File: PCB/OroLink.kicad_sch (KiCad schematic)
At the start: 8 parts, among them J1 67996-408HLF

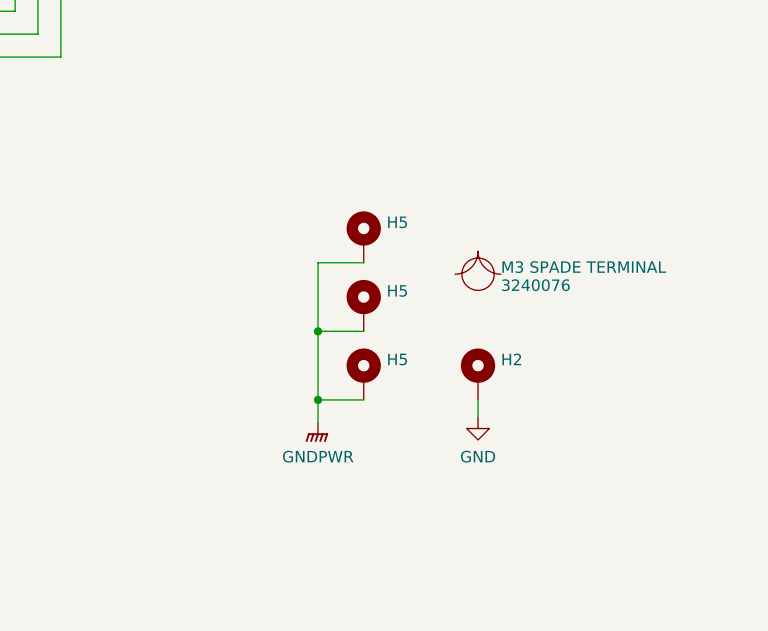
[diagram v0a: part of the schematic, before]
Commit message: add 1nf 3kv caps to GNDPWR mounting holes (closes #29)
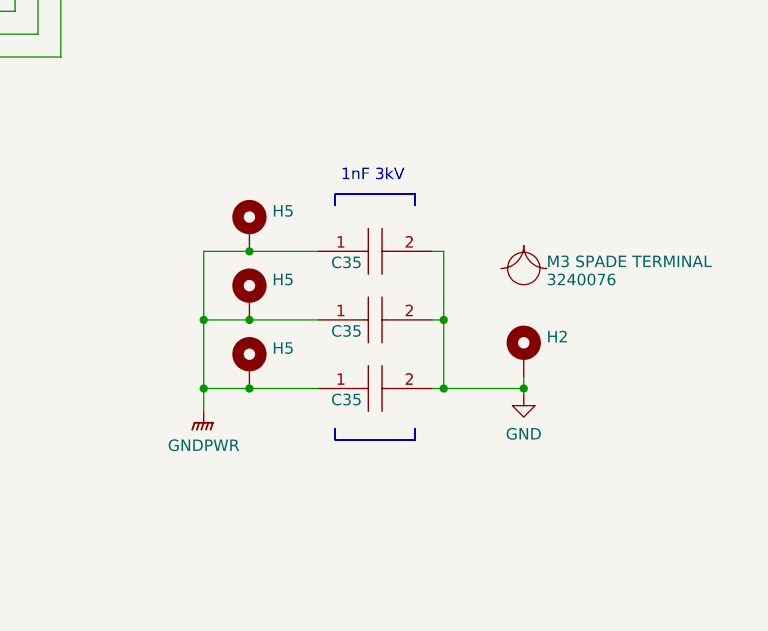
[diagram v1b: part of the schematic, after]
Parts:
- added C35 (x3): 1nF 5kV, CAPC5664X270N, symbol SamacSys_Parts:HV2225Y102KXMATHV
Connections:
- net GND: now also C35.2, C35.2, C35.2
- net GNDPWR: now also C35.1, C35.1, C35.1
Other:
- note added: "1nF 3kV"
- moved on the sheet: H2, H5

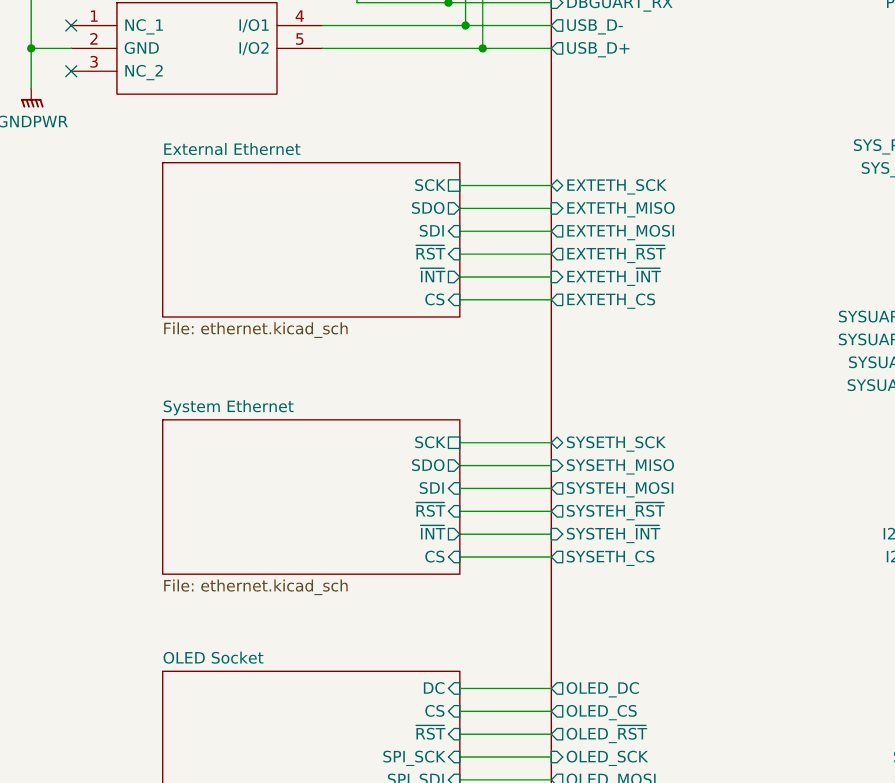
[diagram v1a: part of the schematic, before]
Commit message: switch to self-contained magnetics ethernet jack (closes #28)
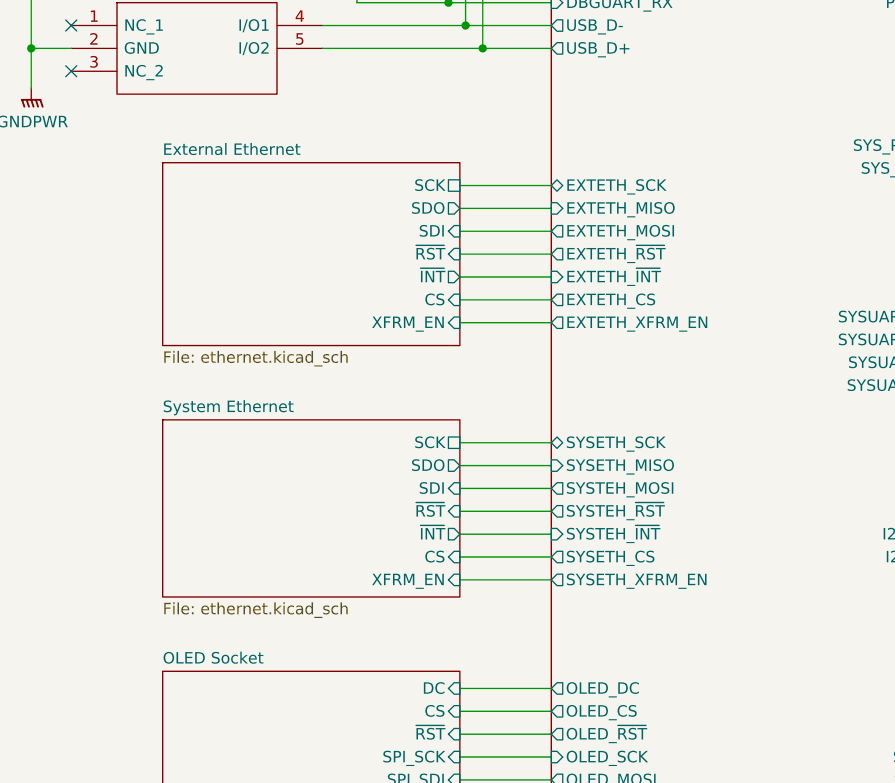
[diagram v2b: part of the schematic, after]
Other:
- sheet External Ethernet ports: added XFRM_EN; removed none
- sheet Microcontroller ports: added EXTETH_XFRM_EN, SYSETH_XFRM_EN; removed none
- sheet System Ethernet ports: added XFRM_EN; removed none
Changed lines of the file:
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@@
+    (stroke (width 0) (type default))
+  )
+  (wire (pts (xy 73.66 119.38) (xy 83.82 119.38))
     (stroke (width 0) (type default))
   )
@@
   )
   (wire (pts (xy 73.66 85.725) (xy 83.82 85.725))
+    (stroke (width 0) (type default))
+  )
+  (wire (pts (xy 73.66 90.805) (xy 83.82 90.805))
     (stroke (width 0) (type default))
   )
@@
     )
   )
-  (sheet (at 40.64 101.6) (size 33.02 17.145) (fields_autoplaced)
+  (sheet (at 40.64 101.6) (size 33.02 19.685) (fields_autoplaced)
     (stroke (width 0.1524) (type solid))
     (fill (color 0 0 0 0.0000))
@@
       (effects (font (size 1.27 1.27)) (justify left bottom))
     )
-    (property "Sheetfile" "ethernet.kicad_sch" (at 40.64 119.3296 0)
+    (property "Sheetfile" "ethernet.kicad_sch" (at 40.64 121.8696 0)
       (effects (font (size 1.27 1.27)) (justify left top))
     )
@@
     )
     (pin "CS" input (at 73.66 116.84 0)
+      (effects (font (size 1.27 1.27)) (justify right))
+    )
+    (pin "XFRM_EN" input (at 73.66 119.38 0)
       (effects (font (size 1.27 1.27)) (justify right))
     )
@@
     )
   )
-  (sheet (at 40.64 73.025) (size 33.02 17.145) (fields_autoplaced)
+  (sheet (at 40.64 73.025) (size 33.02 20.32) (fields_autoplaced)
     (stroke (width 0.1524) (type solid))
     (fill (color 0 0 0 0.0000))
@@
       (effects (font (size 1.27 1.27)) (justify left bottom))
     )
-    (property "Sheetfile" "ethernet.kicad_sch" (at 40.64 90.7546 0)
+    (property "Sheetfile" "ethernet.kicad_sch" (at 40.64 93.9296 0)
       (effects (font (size 1.27 1.27)) (justify left top))
     )
@@
     )
     (pin "CS" input (at 73.66 88.265 0)
+      (effects (font (size 1.27 1.27)) (justify right))
+    )
+    (pin "XFRM_EN" input (at 73.66 90.805 0)
       (effects (font (size 1.27 1.27)) (justify right))
     )
@@
       (effects (font (size 1.27 1.27)) (justify left))
     )
+    (pin "SYSETH_XFRM_EN" output (at 83.82 119.38 180)
+      (effects (font (size 1.27 1.27)) (justify left))
+    )
+    (pin "EXTETH_XFRM_EN" output (at 83.82 90.805 180)
+      (effects (font (size 1.27 1.27)) (justify left))
+    )

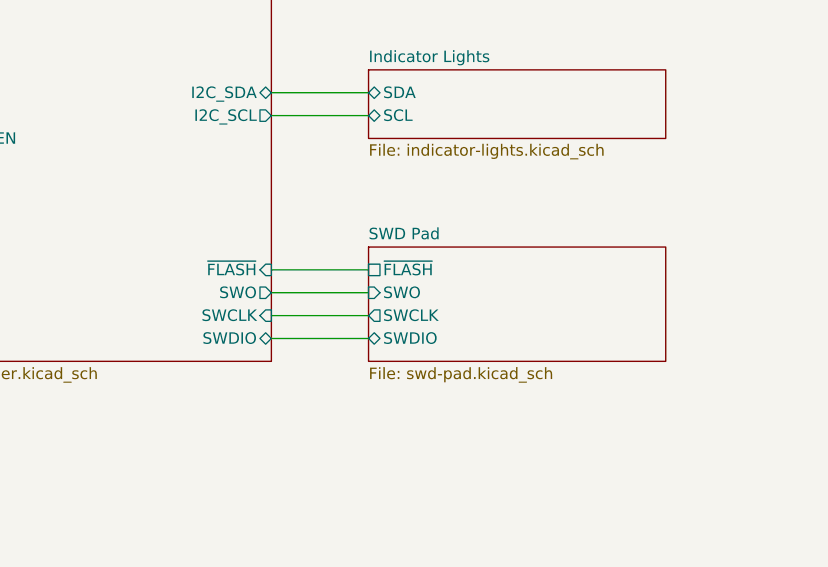
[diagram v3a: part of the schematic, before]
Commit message: add pullup/down resistors and fix oro 6p lines with boot1/0
closes #24
closes #21
closes #15
closes #12
closes #6
closes #3
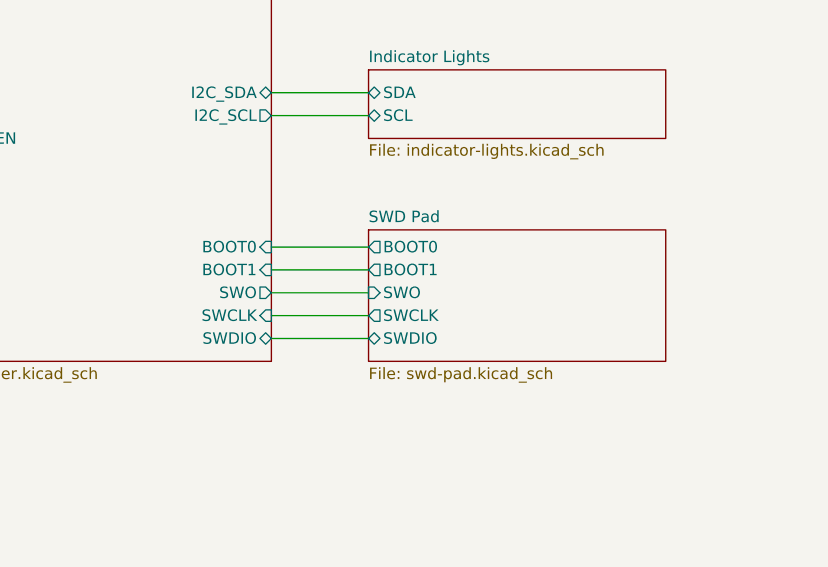
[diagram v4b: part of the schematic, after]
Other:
- sheet Microcontroller ports: added BOOT0, BOOT1; removed ~{FLASH}
- sheet SWD Pad ports: added BOOT0, BOOT1; removed ~{FLASH}
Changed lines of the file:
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@@
+    (stroke (width 0) (type default))
+  )
+  (wire (pts (xy 129.54 131.445) (xy 140.335 131.445))
     (stroke (width 0) (type default))
   )
@@
     )
   )
-  (sheet (at 140.335 131.445) (size 33.02 12.7)
+  (sheet (at 140.335 129.54) (size 33.02 14.605)
     (stroke (width 0.1524) (type solid))
     (fill (color 0 0 0 0.0000))
-    (property "Sheetname" "SWD Pad" (at 140.335 130.7334 0)
+    (property "Sheetname" "SWD Pad" (at 140.335 128.8284 0)
       (effects (font (size 1.27 1.27)) (justify left bottom))
     )
@@
       (effects (font (size 1.27 1.27)) (justify left top))
     )
-    (pin "~{FLASH}" passive (at 140.335 133.985 180)
-      (effects (font (size 1.27 1.27)) (justify left))
-    )
     (pin "SWO" input (at 140.335 136.525 180)
       (effects (font (size 1.27 1.27)) (justify left))
@@
     )
     (pin "SWDIO" bidirectional (at 140.335 141.605 180)
+      (effects (font (size 1.27 1.27)) (justify left))
+    )
+    (pin "BOOT1" output (at 140.335 133.985 180)
+      (effects (font (size 1.27 1.27)) (justify left))
+    )
+    (pin "BOOT0" output (at 140.335 131.445 180)
       (effects (font (size 1.27 1.27)) (justify left))
     )
@@
       (effects (font (size 1.27 1.27)) (justify right))
     )
-    (pin "~{FLASH}" input (at 129.54 133.985 0)
-      (effects (font (size 1.27 1.27)) (justify right))
-    )
     (pin "OLED_MOSI" output (at 83.82 141.605 180)
       (effects (font (size 1.27 1.27)) (justify left))
@@
       (effects (font (size 1.27 1.27)) (justify left))
     )
-    (instances
+    (pin "BOOT0" input (at 129.54 131.445 0)
+      (effects (font (size 1.27 1.27)) (justify right))
+    )
+    (pin "BOOT1" input (at 129.54 133.985 0)
+      (effects (font (size 1.27 1.27)) (justify right))
+    )
+    (instances

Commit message: switch to smaller package for 1nF 3kV caps (closes #33)
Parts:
- C35: footprint CAPC5664X270N -> CAPC4620X220N; symbol SamacSys_Parts:HV2225Y102KXMATHV -> SamacSys_Parts:885342210004; Height 2.7 -> 2.2; Manufacturer_Name Vishay -> Wurth Elektronik; Manufacturer_Part_Number HV2225Y102KXMATHV -> 885342210004; Mouser Part Number 77-HV2225Y102KXMATHV -> 710-885342210004; Mouser Price/Stock https://www.mouser.com/Search/Refine.aspx?Keyword=77-HV2225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 -> https://www.mouser.co.uk/ProductDetail/Wurth-Elektronik/885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
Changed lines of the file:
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@@
     )
   )
-  (symbol (lib_id "SamacSys_Parts:HV2225Y102KXMATHV") (at 222.25 119.38 0) (unit 1)
+  (symbol (lib_id "SamacSys_Parts:885342210004") (at 222.25 119.38 0) (unit 1)
     (in_bom yes) (on_board yes) (dnp no)
     (property "Reference" "C35" (at 225.425 120.65 0)
@@
       (effects (font (size 1.27 1.27)) hide)
     )
-    (property "Footprint" "CAPC5664X270N" (at 231.14 118.11 0)
-      (effects (font (size 1.27 1.27)) (justify left) hide)
-    )
-    (property "Datasheet" "https://componentsearchengine.com/Datasheets/1/HV2225Y102KXMATHV.pdf" (at 231.14 120.65 0)
-      (effects (font (size 1.27 1.27)) (justify left) hide)
-    )
-    (property "Description" "Multilayer Ceramic Capacitors MLCC - SMD/SMT 1.0nF 5000volts 10% X7R High Voltage" (at 231.14 123.19 0)
-      (effects (font (size 1.27 1.27)) (justify left) hide)
-    )
-    (property "Height" "2.7" (at 231.14 125.73 0)
-      (effects (font (size 1.27 1.27)) (justify left) hide)
-    )
-    (property "Manufacturer_Name" "Vishay" (at 231.14 128.27 0)
-      (effects (font (size 1.27 1.27)) (justify left) hide)
-    )
-    (property "Manufacturer_Part_Number" "HV2225Y102KXMATHV" (at 231.14 130.81 0)
-      (effects (font (size 1.27 1.27)) (justify left) hide)
-    )
-    (property "Mouser Part Number" "77-HV2225Y102KXMATHV" (at 231.14 133.35 0)
-      (effects (font (size 1.27 1.27)) (justify left) hide)
-    )
-    (property "Mouser Price/Stock" "https://www.mouser.com/Search/Refine.aspx?Keyword=77-HV2225Y102KXMATHV" (at 231.14 135.89 0)
+    (property "Footprint" "CAPC4620X220N" (at 231.14 118.11 0)
+      (effects (font (size 1.27 1.27)) (justify left) hide)
+    )
+    (property "Datasheet" "https://katalog.we-online.com/pbs/datasheet/885342210004.pdf" (at 231.14 120.65 0)
+      (effects (font (size 1.27 1.27)) (justify left) hide)
+    )
+    (property "Description" "Multilayer Ceramic Chip Capacitor WCAP-CSMH Series 1808 1000pF X7R1808102KC00DFCT10000" (at 231.14 123.19 0)
+      (effects (font (size 1.27 1.27)) (justify left) hide)
+    )
+    (property "Height" "2.2" (at 231.14 125.73 0)
+      (effects (font (size 1.27 1.27)) (justify left) hide)
+    )
+    (property "Manufacturer_Name" "Wurth Elektronik" (at 231.14 128.27 0)
+      (effects (font (size 1.27 1.27)) (justify left) hide)
+    )
+    (property "Manufacturer_Part_Number" "885342210004" (at 231.14 130.81 0)
+      (effects (font (size 1.27 1.27)) (justify left) hide)
+    )
+    (property "Mouser Part Number" "710-885342210004" (at 231.14 133.35 0)
+      (effects (font (size 1.27 1.27)) (justify left) hide)
+    )
+    (property "Mouser Price/Stock" "https://www.mouser.co.uk/ProductDetail/Wurth-Elektronik/885342210004?qs=MLItCLRbWsya%2F3qdX09FHQ%3D%3D" (at 231.14 135.89 0)
       (effects (font (size 1.27 1.27)) (justify left) hide)
     )
@@
     )
   )
-  (symbol (lib_id "SamacSys_Parts:HV2225Y102KXMATHV") (at 222.25 127 0) (unit 1)
+  (symbol (lib_id "SamacSys_Parts:885342210004") (at 222.25 127 0) (unit 1)
     (in_bom yes) (on_board yes) (dnp no)
     (property "Reference" "C35" (at 225.425 128.27 0)
@@
       (effects (font (size 1.27 1.27)) hide)
     )
-    (property "Footprint" "CAPC5664X270N" (at 231.14 125.73 0)
-      (effects (font (size 1.27 1.27)) (justify left) hide)
-    )
-    (property "Datasheet" "https://componentsearchengine.com/Datasheets/1/HV2225Y102KXMATHV.pdf" (at 231.14 128.27 0)
-      (effects (font (size 1.27 1.27)) (justify left) hide)
-    )
-    (property "Description" "Multilayer Ceramic Capacitors MLCC - SMD/SMT 1.0nF 5000volts 10% X7R High Voltage" (at 231.14 130.81 0)
-      (effects (font (size 1.27 1.27)) (justify left) hide)
-    )
-    (property "Height" "2.7" (at 231.14 133.35 0)
-      (effects (font (size 1.27 1.27)) (justify left) hide)
-    )
-    (property "Manufacturer_Name" "Vishay" (at 231.14 135.89 0)
-      (effects (font (size 1.27 1.27)) (justify left) hide)
-    )
-    (property "Manufacturer_Part_Number" "HV2225Y102KXMATHV" (at 231.14 138.43 0)
-      (effects (font (size 1.27 1.27)) (justify left) hide)
-    )
-    (property "Mouser Part Number" "77-HV2225Y102KXMATHV" (at 231.14 140.97 0)
-      (effects (font (size 1.27 1.27)) (justify left) hide)
-    )
-    (property "Mouser Price/Stock" "https://www.mouser.com/Search/Refine.aspx?Keyword=77-HV2225Y102KXMATHV" (at 231.14 143.51 0)
+    (property "Footprint" "CAPC4620X220N" (at 231.14 125.73 0)
+      (effects (font (size 1.27 1.27)) (justify left) hide)
+    )
+    (property "Datasheet" "https://katalog.we-online.com/pbs/datasheet/885342210004.pdf" (at 231.14 128.27 0)
+      (effects (font (size 1.27 1.27)) (justify left) hide)
+    )
+    (property "Description" "Multilayer Ceramic Chip Capacitor WCAP-CSMH Series 1808 1000pF X7R1808102KC00DFCT10000" (at 231.14 130.81 0)
+      (effects (font (size 1.27 1.27)) (justify left) hide)
+    )
+    (property "Height" "2.2" (at 231.14 133.35 0)
+      (effects (font (size 1.27 1.27)) (justify left) hide)
+    )
+    (property "Manufacturer_Name" "Wurth Elektronik" (at 231.14 135.89 0)
+      (effects (font (size 1.27 1.27)) (justify left) hide)
+    )
+    (property "Manufacturer_Part_Number" "885342210004" (at 231.14 138.43 0)
+      (effects (font (size 1.27 1.27)) (justify left) hide)
+    )
+    (property "Mouser Part Number" "710-885342210004" (at 231.14 140.97 0)
+      (effects (font (size 1.27 1.27)) (justify left) hide)
+    )
+    (property "Mouser Price/Stock" "https://www.mouser.co.uk/ProductDetail/Wurth-Elektronik/885342210004?qs=MLItCLRbWsya%2F3qdX09FHQ%3D%3D" (at 231.14 143.51 0)
       (effects (font (size 1.27 1.27)) (justify left) hide)
     )
@@
     )
   )
-  (symbol (lib_id "SamacSys_Parts:HV2225Y102KXMATHV") (at 222.25 134.62 0) (unit 1)
+  (symbol (lib_id "SamacSys_Parts:885342210004") (at 222.25 134.62 0) (unit 1)
     (in_bom yes) (on_board yes) (dnp no)
     (property "Reference" "C35" (at 225.425 135.89 0)
@@
       (effects (font (size 1.27 1.27)) hide)
     )
-    (property "Footprint" "CAPC5664X270N" (at 231.14 133.35 0)
-      (effects (font (size 1.27 1.27)) (justify left) hide)
-    )
-    (property "Datasheet" "https://componentsearchengine.com/Datasheets/1/HV2225Y102KXMATHV.pdf" (at 231.14 135.89 0)
-      (effects (font (size 1.27 1.27)) (justify left) hide)
-    )
-    (property "Description" "Multilayer Ceramic Capacitors MLCC - SMD/SMT 1.0nF 5000volts 10% X7R High Voltage" (at 231.14 138.43 0)
-      (effects (font (size 1.27 1.27)) (justify left) hide)
-    )
-    (property "Height" "2.7" (at 231.14 140.97 0)
-      (effects (font (size 1.27 1.27)) (justify left) hide)
-    )
-    (property "Manufacturer_Name" "Vishay" (at 231.14 143.51 0)
-      (effects (font (size 1.27 1.27)) (justify left) hide)
-    )
-    (property "Manufacturer_Part_Number" "HV2225Y102KXMATHV" (at 231.14 146.05 0)
-      (effects (font (size 1.27 1.27)) (justify left) hide)
-    )
-    (property "Mouser Part Number" "77-HV2225Y102KXMATHV" (at 231.14 148.59 0)
-      (effects (font (size 1.27 1.27)) (justify left) hide)
-    )
-    (property "Mouser Price/Stock" "https://www.mouser.com/Search/Refine.aspx?Keyword=77-HV2225Y102KXMATHV" (at 231.14 151.13 0)
-      (effects (font (size 1.27 1.27)) (justify left) hide)
-    )
+    (property "Footprint" "CAPC4620X220N" (at 231.14 133.35 0)
+      (effects (font (size 1.27 1.27)) (justify left) hide)
+    )
+    (property "Datasheet" "https://katalog.we-online.com/pbs/datasheet/885342210004.pdf" (at 231.14 135.89 0)
+      (effects (font (size 1.27 1.27)) (justify left) hide)
+    )
+    (property "Description" "Multilayer Ceramic Chip Capacitor WCAP-CSMH Series 1808 1000pF X7R1808102KC00DFCT10000" (at 231.14 138.43 0)
+      (effects (font (size 1.27 1.27)) (justify left) hide)
+    )
+    (property "Height" "2.2" (at 231.14 140.97 0)
+      (effects (font (size 1.27 1.27)) (justify left) hide)
+    )
+    (property "Manufacturer_Name" "Wurth Elektronik" (at 231.14 143.51 0)
+      (effects (font (size 1.27 1.27)) (justify left) hide)
+    )
+    (property "Manufacturer_Part_Number" "885342210004" (at 231.14 146.05 0)
+      (effects (font (size 1.27 1.27)) (justify left) hide)
+    )
+    (property "Mouser Part Number" "710-885342210004" (at 231.14 148.59 0)
+      (effects (font (size 1.27 1.27)) (justify left) hide)
+    )
+    (property "Mouser Price/Stock" "https://www.mouser.co.uk/ProductDetail/Wurth-Elektronik/885342210004?qs=MLItCLRbWsya%2F3qdX09FHQ%3D%3D" (at 231.14 151.13 0)
+      (effects (font (size 1.27 1.27)) (justify left) hide)
+    )
